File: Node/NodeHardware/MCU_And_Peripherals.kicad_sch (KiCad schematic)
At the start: 97 parts, among them Q1 IRF9540, Q3 2N7002, Q4 2N7002, SW1 RST, SW2 BOOT, SW3 BTN, U1 SIM7000G_DEVBoard, U6 ESP32-S3-WROOM-1, U7 UCC27511ADBV

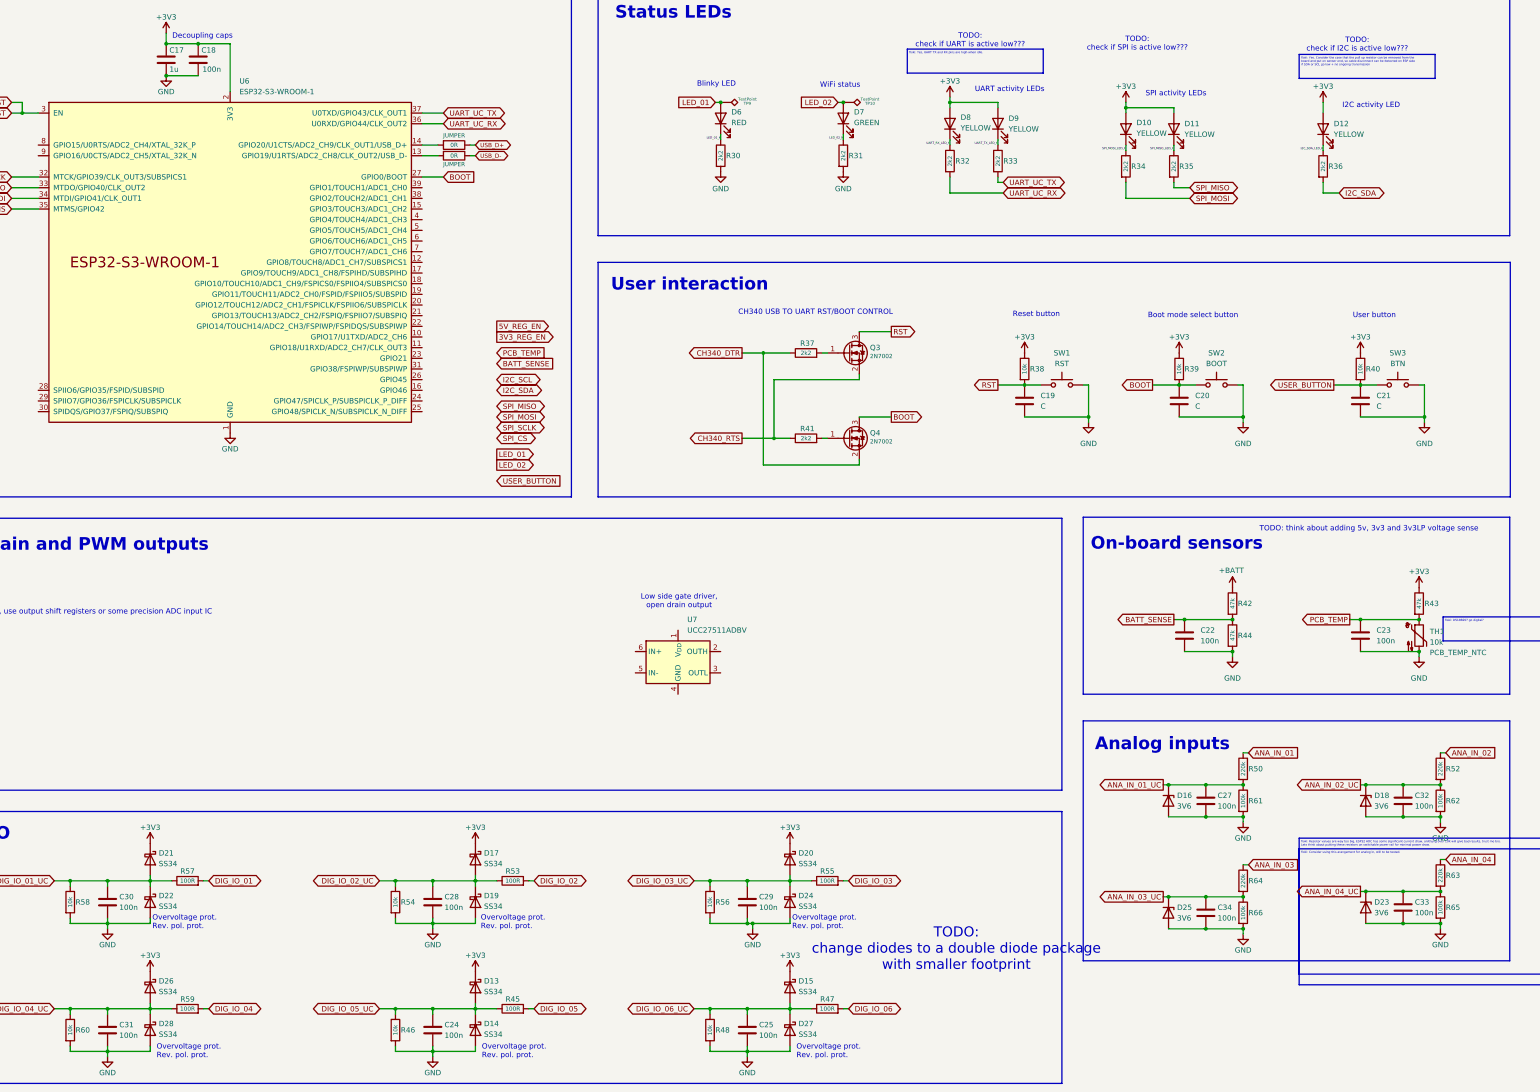
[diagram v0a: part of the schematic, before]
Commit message: Cleanup and update gitignore
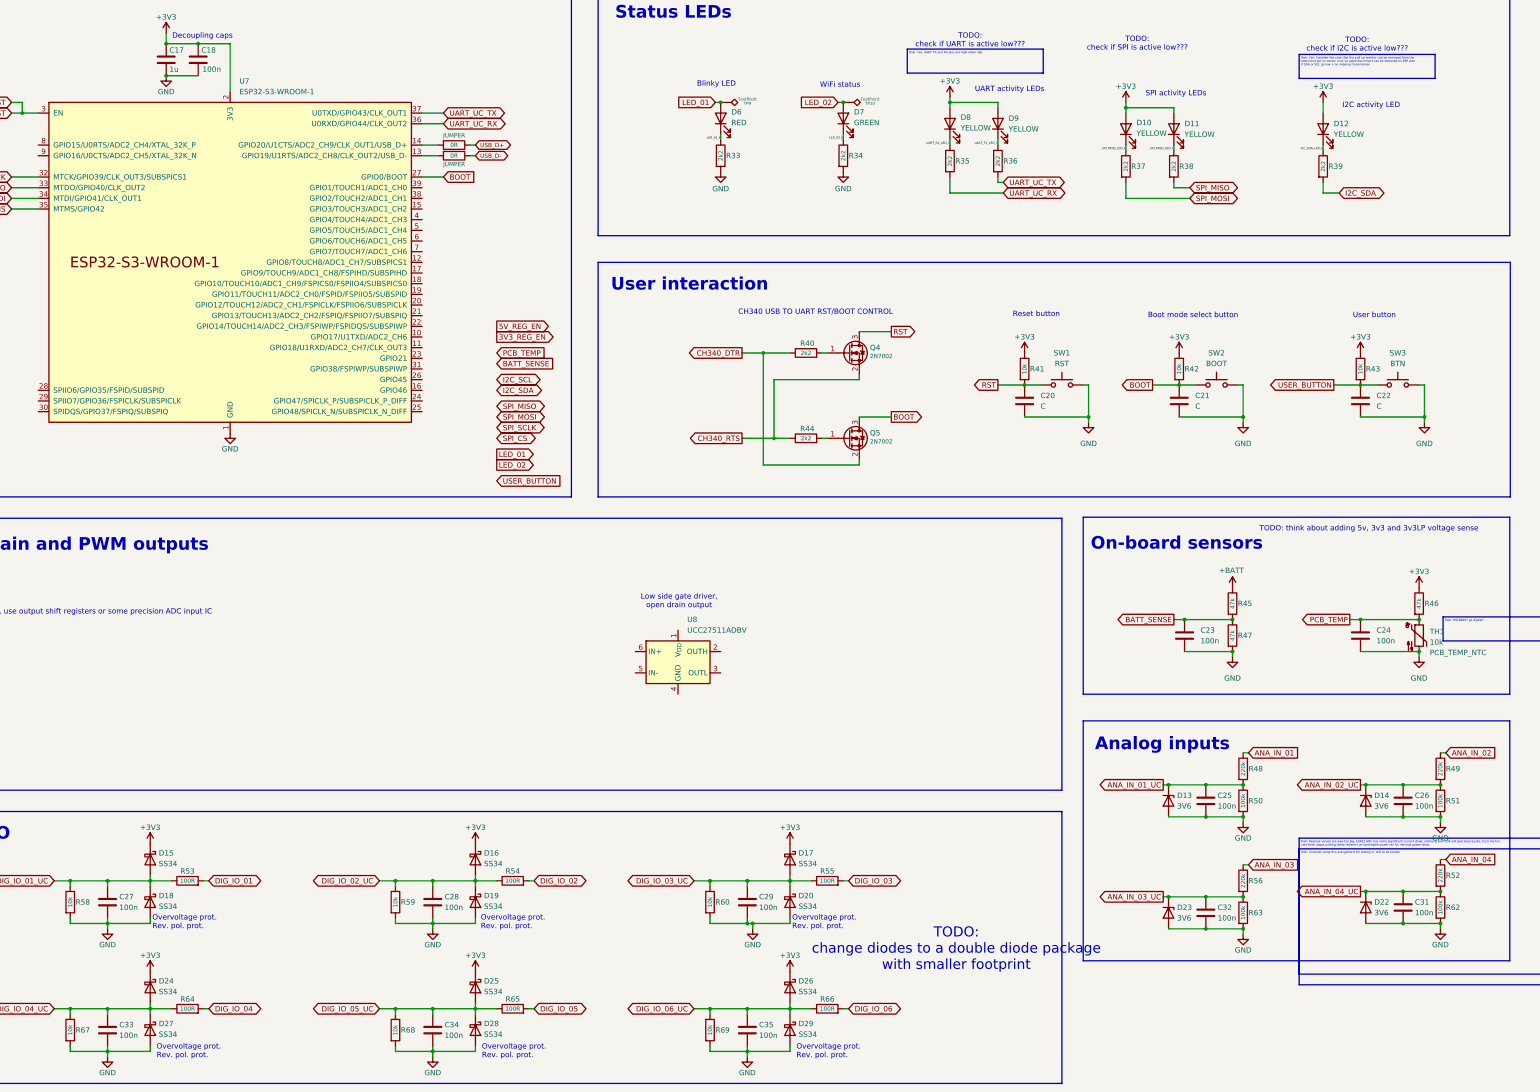
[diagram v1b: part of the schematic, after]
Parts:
- renumbered C19 to C20, C20 to C21, C21 to C22, C22 to C23, C23 to C24, C27 to C25, C32 to C26, C30 to C27, C33 to C31, C34 to C32, C31 to C33, C24 to C34, C25 to C35, D16 to D13, D18 to D14, D21 to D15, D17 to D16, D20 to D17, D22 to D18, D24 to D20, D23 to D22, D25 to D23, D26 to D24, D13 to D25, D15 to D26, D28 to D27, D14 to D28, D27 to D29, Q3 to Q4, Q4 to Q5, R28 to R29, R29 to R32, R30 to R33, R31 to R34, R32 to R35, R33 to R36, R34 to R37, R35 to R38, R36 to R39, R37 to R40, R38 to R41, R39 to R42, R40 to R43, R41 to R44, R42 to R45, R43 to R46, R44 to R47, R50 to R48, R52 to R49, R61 to R50, R62 to R51, R63 to R52, R57 to R53, R53 to R54, R64 to R56, R54 to R59, R56 to R60, R65 to R62, R66 to R63, R59 to R64, R45 to R65, R47 to R66, R60 to R67, R46 to R68, R48 to R69, U6 to U7, U7 to U8

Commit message: Schm cleanup and commenting
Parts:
- removed C1: 100n, Capacitor_SMD:C_1206_3216Metric_Pad1.42x1.75mm_HandSolder, symbol Device:C
- removed C2: 1000u16V, myComponents:CAP_Radial_D10.0mm_P5.00mm, symbol Device:CP1
- removed D1: 3V6, Diode_SMD:D_SOD-123, symbol Device:D_Zener
- removed Q1: IRF9540, myComponents:TO-220-3_SolderedTab, symbol Device:Q_PMOS_GDS
- removed R1: 10K, Resistor_SMD:R_0805_2012Metric_Pad1.15x1.40mm_HandSolder, symbol Device:R
- removed R2: 470R, Resistor_SMD:R_0805_2012Metric_Pad1.15x1.40mm_HandSolder, symbol Device:R
- removed R3, R4, R5: 10K, Resistor_SMD:R_0805_2012Metric_Pad1.20x1.40mm_HandSolder, symbol Device:R
- removed U1: SIM7000G_DEVBoard, myComponents:sim7000G_dev_board_rev3, symbol myComponents:SIM7000G_DEVBoard
- R33, R34, R35, R36, R38, R39: value 2k2 -> 10k
- R37: value 2k2 -> 10kk
- R48, R49, R52, R56: value 220k -> 470R
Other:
- note removed: "I2C activity LED"
- note removed: "SPI activity LEDs"
- note removed: "TODO: change diodes to a double diode package with smaller footprint"
- note removed: "TODO: check if I2C is active low???"
- note removed: "TODO: check if UART is active low???"
- note removed: "UART activity LEDs"
- moved on the sheet: D10, D11, D12, D6, D7, D8, D9, R33, R34, R35, R36, R37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
